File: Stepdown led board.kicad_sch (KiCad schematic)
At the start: 5 parts, among them J1 In, J2 Out, J3 Stepdown

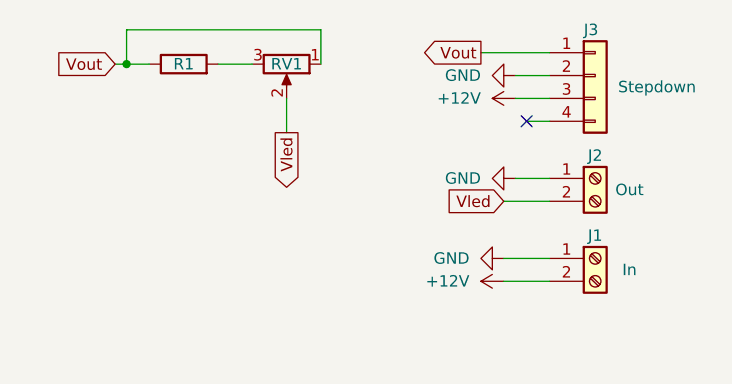
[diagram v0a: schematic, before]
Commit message: - v1.1 (shorter version with component on both sides (WIP) - Reorganized production files folders
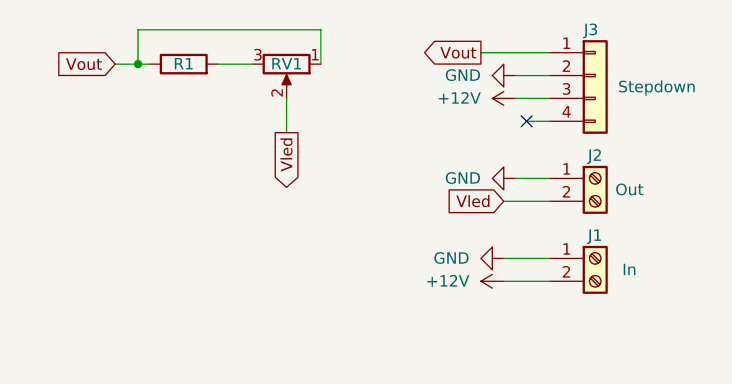
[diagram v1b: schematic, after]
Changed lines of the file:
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@@
 (kicad_sch (version 20211123) (generator eeschema)
   (paper "A4")
-  (junction (at 26.67 21.59) (diameter 0) (color 0 0 0 0)
+  (junction (at 27.94 21.59) (diameter 0) (color 0 0 0 0)
   )
   (no_connect (at 71.12 27.94))
-  (wire (pts (xy 48.26 21.59) (xy 48.26 17.78))
+  (wire (pts (xy 27.94 21.59) (xy 29.21 21.59))
     (stroke (width 0) (type default) (color 0 0 0 0))
   )
@@
     (stroke (width 0) (type default) (color 0 0 0 0))
   )
-  (wire (pts (xy 26.67 17.78) (xy 26.67 21.59))
+  (wire (pts (xy 48.26 17.78) (xy 27.94 17.78))
+    (stroke (width 0) (type default) (color 0 0 0 0))
+  )
+  (wire (pts (xy 36.83 21.59) (xy 40.64 21.59))
     (stroke (width 0) (type default) (color 0 0 0 0))
   )
@@
   )
   (wire (pts (xy 73.66 45.72) (xy 68.58 45.72))
-    (stroke (width 0) (type default) (color 0 0 0 0))
-  )
-  (wire (pts (xy 48.26 17.78) (xy 26.67 17.78))
-    (stroke (width 0) (type default) (color 0 0 0 0))
-  )
-  (wire (pts (xy 26.67 21.59) (xy 29.21 21.59))
     (stroke (width 0) (type default) (color 0 0 0 0))
   )
@@
     (stroke (width 0) (type default) (color 0 0 0 0))
   )
+  (wire (pts (xy 27.94 17.78) (xy 27.94 21.59))
+    (stroke (width 0) (type default) (color 0 0 0 0))
+  )
+  (wire (pts (xy 48.26 21.59) (xy 48.26 17.78))
+    (stroke (width 0) (type default) (color 0 0 0 0))
+  )
   (wire (pts (xy 66.04 20.32) (xy 73.66 20.32))
     (stroke (width 0) (type default) (color 0 0 0 0))
@@
     (stroke (width 0) (type default) (color 0 0 0 0))
   )
-  (wire (pts (xy 25.4 21.59) (xy 26.67 21.59))
+  (wire (pts (xy 25.4 21.59) (xy 27.94 21.59))
     (stroke (width 0) (type default) (color 0 0 0 0))
   )
-  (wire (pts (xy 36.83 21.59) (xy 40.64 21.59))
-    (stroke (width 0) (type default) (color 0 0 0 0))
-  )

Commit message: Version 1.1.0 WIP
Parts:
- J1: value In -> IN
- J2: value Out -> OUT
- R1: footprint Resistor_THT:R_Axial_DIN0204_L3.6mm_D1.6mm_P7.62mm_Horizontal -> Resistor_SMD:R_2816_7142Metric_Pad3.20x4.45mm_HandSolder
- RV1: footprint Potentiometer_THT:Potentiometer_ACP_CA9-V10_Vertical -> Potentiometer_SMD:Potentiometer_ACP_CA6-VSMD_Vertical
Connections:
- net +12V: now also J3.2 (Pin_2); no longer J3.3 (Pin_3)
- net GND: now also J3.3 (Pin_3), R1.2, RV1.1; no longer J2.1 (Pin_1), J3.2 (Pin_2)
- net Vout: now also J3.4 (Pin_4), RV1.3; no longer J3.1 (Pin_1), R1.1, RV1.1
- new net: J2.1 (Pin_1), R1.1
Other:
- moved on the sheet: R1, RV1

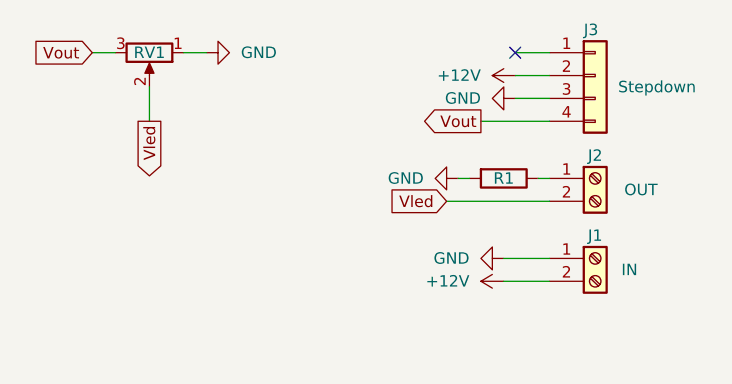
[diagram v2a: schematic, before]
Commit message: - Schematic cleanup - Layout (silk) update
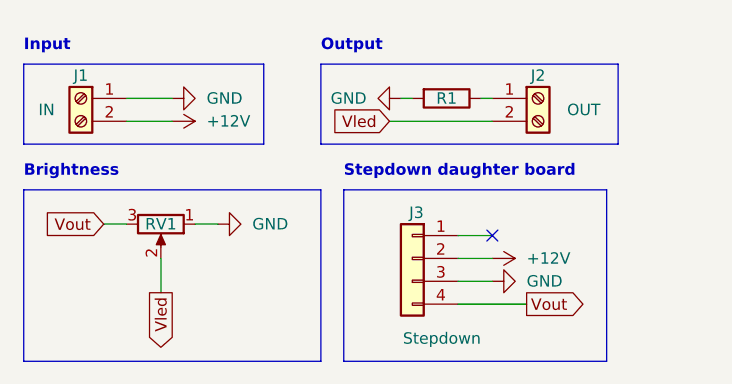
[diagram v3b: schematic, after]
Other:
- note added: "Brightness"
- note added: "Input"
- note added: "Output"
- note added: "Stepdown daughter board"
- company: (none) -> BrokenPipe
- title: (none) -> Led dimmer board
- moved on the sheet: J1, J2, J3, R1, RV1
